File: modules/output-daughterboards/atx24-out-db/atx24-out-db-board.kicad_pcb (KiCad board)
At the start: 4 copper layers, 238 x 77 mm, 15 parts, among them J1 ATX24 OUT FIELD, J10 TE 63849-1, J11 TE 63849-1, J12 TE 63849-1, J13 TE 63849-1, J14 TE 63849-1, J15 TE 63849-1, J16 TE 63849-1, J17 TE 63849-1, J18 TE 63849-1, J20 SIGNAL STUB (2x5)

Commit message: WIP snapshot: daughterboard-projects agent in flight (durability)
Co-Authored-By: Claude Fable 5 <noreply@anthropic.com>
Claude-Session: https://claude.ai/code/session_01LvfqcnEeuin2oyJQw548EX
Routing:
- net +5V: track 138.7 -> 148.9 mm
- net +12V: track 66.2 -> 71.3 mm
- net +5VSB: track 49.1 -> 54.2 mm
- net +3V3: track 114.7 -> 119.8 mm

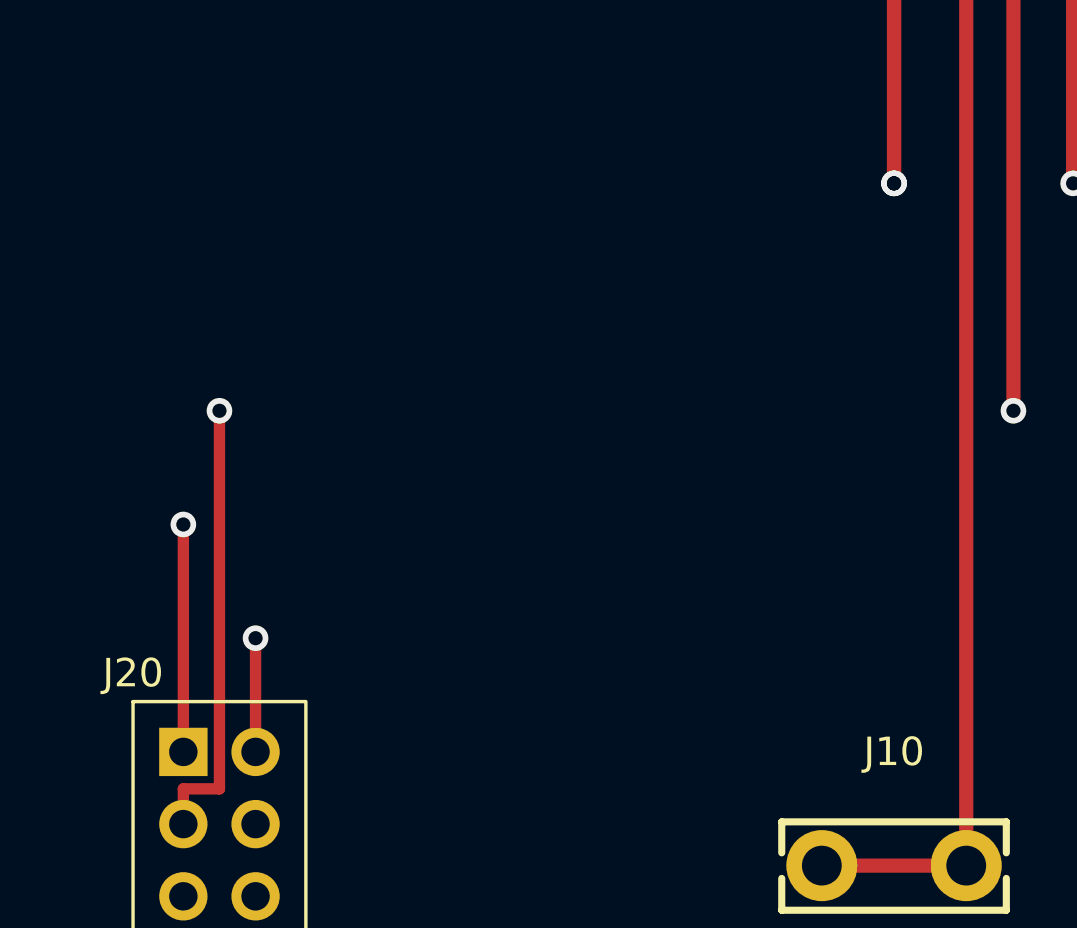
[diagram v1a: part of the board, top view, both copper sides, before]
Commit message: Task 10: output-daughterboard projects landed (atx24/eps/pcie, SS2.8 v1.4.0)
Three passive per-cable boards: TE 63849-1 tabs mapped 1:1 to the main
boards' TB order (a pin swap caught+fixed by cross-ref), full TH output
fields (24-circuit ATX / EPS 4+4 / PCIe 3+3+2sense-tied-GND), asymmetric
keying verified programmatically distinct across families, M3 chassis
mounts. 4-layer 2oz: EPS/PCIe = zero-track pure-pour 2-net boards; atx24 =
8-net In2 band routing (stale-netlist silent-reassignment bug found+fixed).
ERC 0 errors / DRC 0 at every severity, netlist-verified by
check_output_daughterboards.py. MODDIY not invented (OQ-88 provenance);
sense-return provisioned only (box e open). New lib assets + parametric
generator + check script.

Co-Authored-By: Claude Fable 5 <noreply@anthropic.com>
Claude-Session: https://claude.ai/code/session_01LvfqcnEeuin2oyJQw548EX
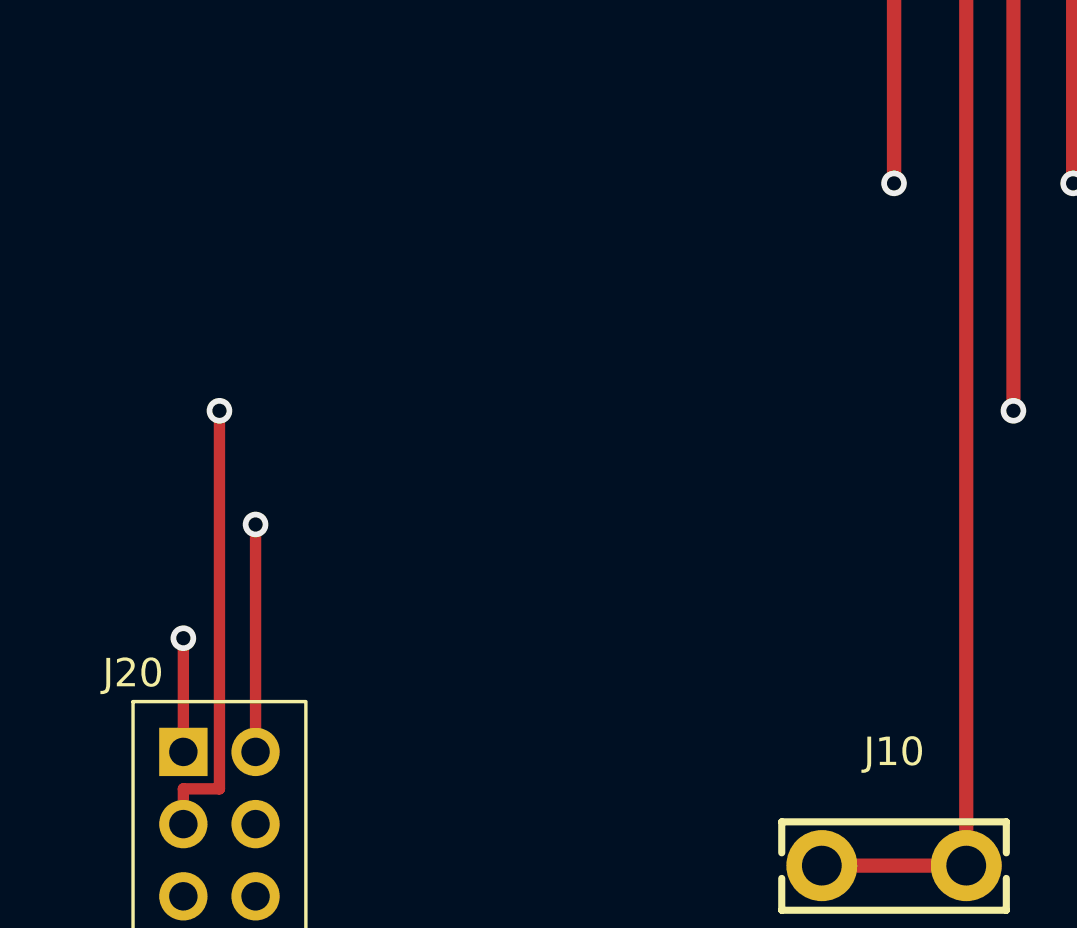
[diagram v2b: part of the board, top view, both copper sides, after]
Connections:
- J20 pad 1: /PWR_OK -> /PS_ON#
- J20 pad 2: /PS_ON# -> /PWR_OK
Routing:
- net +3V3: vias 5 -> 4

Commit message: Bench-mode Max addendum: T1 carries continuous telemetry, bursts for raw; GOWIN+P4 hub shape
Sustained budget 180-900 kB/s (10-50kHz/ch decimated) = 1.6-8% of one
100BASE-T1 link; fast-path raw-window bursts land <1s; continuous instrument
raw (100-260 MB/s at the ruled ADC options) exceeds every link class incl.
1000BASE-T1 — the ruled shape stays burst-into-memory, matching SS6.11's own
framing. Max hub ranked: GOWIN GW5A + P4 (owner prototype lineage) >
PolarFire ENT-posture variant > P4-only (OQ-20 caps N=1). GbE/RGMII egress
over USB HS at N=8. Freshness gaps corroborated (SS6.11 retired mux array +
debunked 2-5MHz band already owner-pen-tracked; phantom 'companion FPGA-Max
doc' cited 3x, absent). 8 owner questions incl. a REAL mismatch: owner fast
ADC = two CURRENT pairs (shunt+coil) vs the June-11 ruling's voltage+current
— where does the ATX-ripple VOLTAGE channel live?

Co-Authored-By: Claude Fable 5 <noreply@anthropic.com>
Claude-Session: https://claude.ai/code/session_01LvfqcnEeuin2oyJQw548EX
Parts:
- removed H1, H2, H3, H4: MountingHole_3.2mm_M3_Pad_Via, cec-MountingHole:MountingHole_3.2mm_M3_Pad_Via
- moved J18 145.1 mm to (73.8, 15.0)
- moved J17 144.7 mm to (65.2, 15.0)
- moved J16 144.3 mm to (56.6, 15.0)
- moved J15 143.9 mm to (48.0, 15.0)
- moved J14 129.5 mm to (39.4, 15.0)
- moved J13 115.2 mm to (30.8, 15.0)
- moved J12 101.4 mm to (22.2, 15.0)
- moved J11 101.0 mm to (13.6, 15.0)
- moved J20 62.9 mm to (56.6, 6.77), turned to 90 degrees
- moved J10 61.7 mm to (4.96, 15.0)
- moved J1 42.7 mm to (4.10, 2.75)
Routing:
- net +5V: track 148.9 -> 47.1 mm
- net +3V3: track 119.8 -> 42.8 mm
- net +12V: track 71.3 -> 29.9 mm
- net +5VSB: track 54.2 -> 19.5 mm
- net /-12V: track 41.3 -> 9.88 mm
- net /PS_ON#: track 37.5 -> 11.5 mm
- net /PWR_OK: track 45.1 -> 21.3 mm
- added copper zone on B.Cu, net +5V
- added copper zone on B.Cu, net +5VSB
- added copper zone on B.Cu, net /PWR_OK
- removed copper zone on In2.Cu, net +5V
- removed copper zone on In2.Cu, net +5VSB
- removed copper zone on In2.Cu, net /PWR_OK
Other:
- board size 238 x 77 mm -> 78.7 x 17 mm

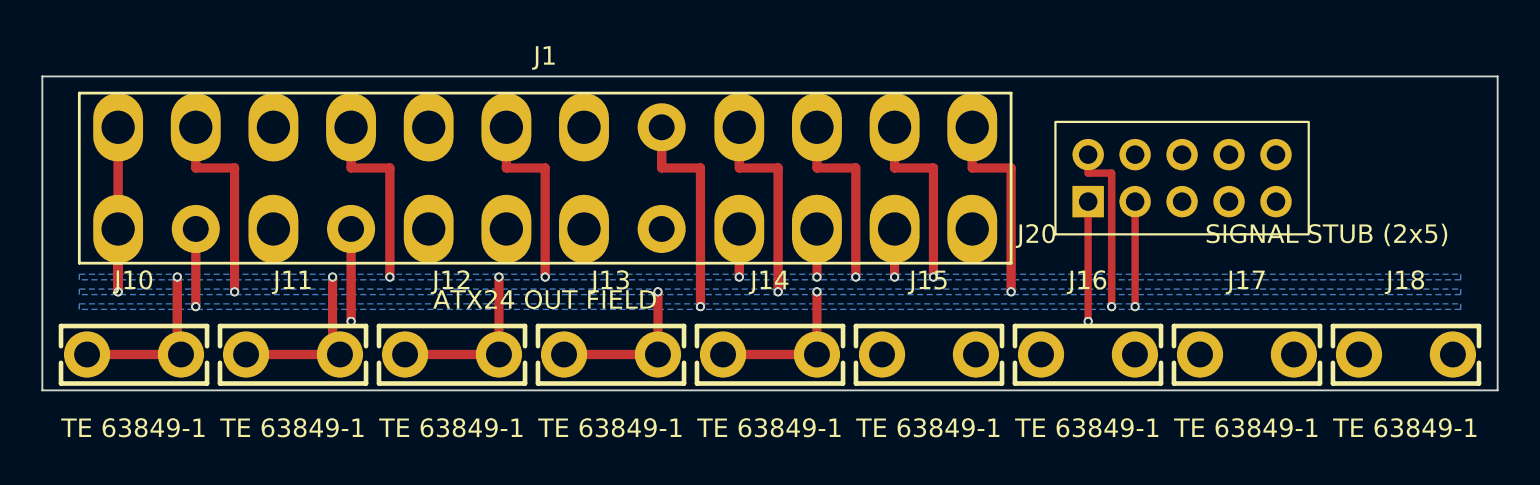
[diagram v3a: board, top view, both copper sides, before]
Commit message: WIP snapshot: shrink + voltage-path agents in flight (durability)
Co-Authored-By: Claude Fable 5 <noreply@anthropic.com>
Claude-Session: https://claude.ai/code/session_01LvfqcnEeuin2oyJQw548EX
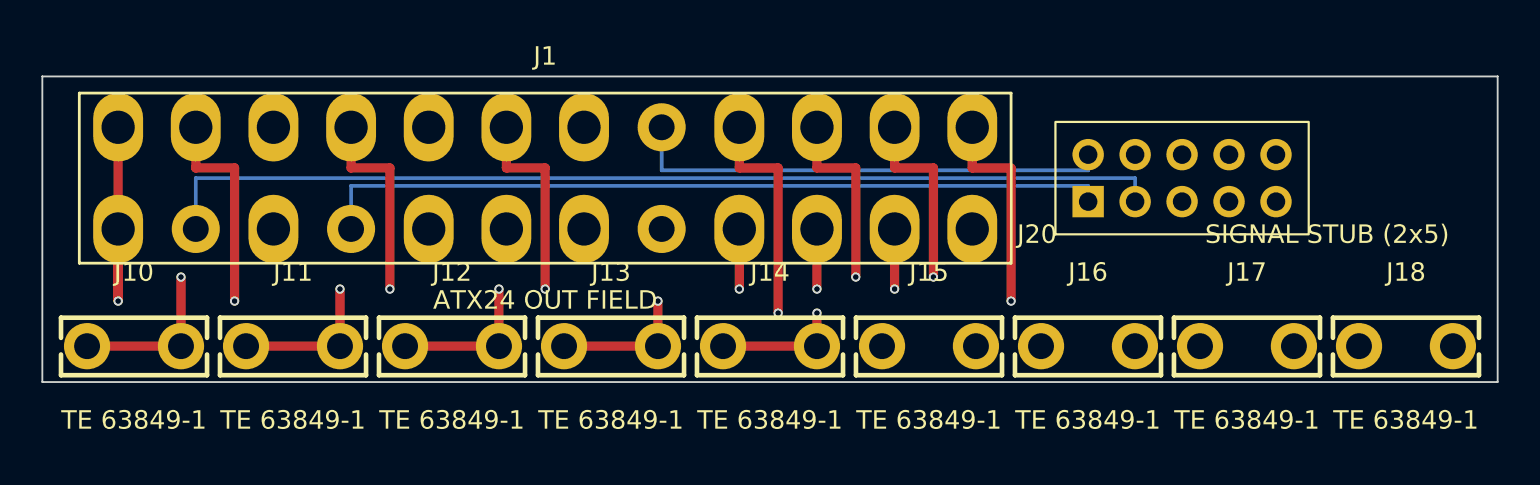
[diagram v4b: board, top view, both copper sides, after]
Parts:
- moved J10 0.45 mm to (4.96, 14.6)
- moved J11 0.45 mm to (13.6, 14.6)
- moved J12 0.45 mm to (22.2, 14.6)
- moved J13 0.45 mm to (30.8, 14.6)
- moved J14 0.45 mm to (39.4, 14.6)
- moved J15 0.45 mm to (48.0, 14.6)
- moved J16 0.45 mm to (56.6, 14.6)
- moved J17 0.45 mm to (65.2, 14.6)
- moved J18 0.45 mm to (73.8, 14.6)
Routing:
- net /-12V: track 9.88 -> 54.8 mm, vias 2 -> 0
- net /PS_ON#: track 11.5 -> 43.1 mm, vias 2 -> 0
- net /PWR_OK: track 21.3 -> 26.2 mm, vias 2 -> 0
- net +3V3: track 42.8 -> 43.8 mm
- net +5V: track 47.1 -> 47.8 mm
- net +12V: track 29.9 -> 29.2 mm
- added copper zone on In2.Cu, net +5V
- added copper zone on In2.Cu, net +5VSB
- removed copper zone on B.Cu, net +5V
- removed copper zone on B.Cu, net +5VSB
- removed copper zone on In2.Cu, net /-12V
- removed copper zone on In2.Cu, net /PS_ON#
- removed copper zone on B.Cu, net /PWR_OK
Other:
- board size 78.7 x 17 mm -> 78.7 x 16.5 mm

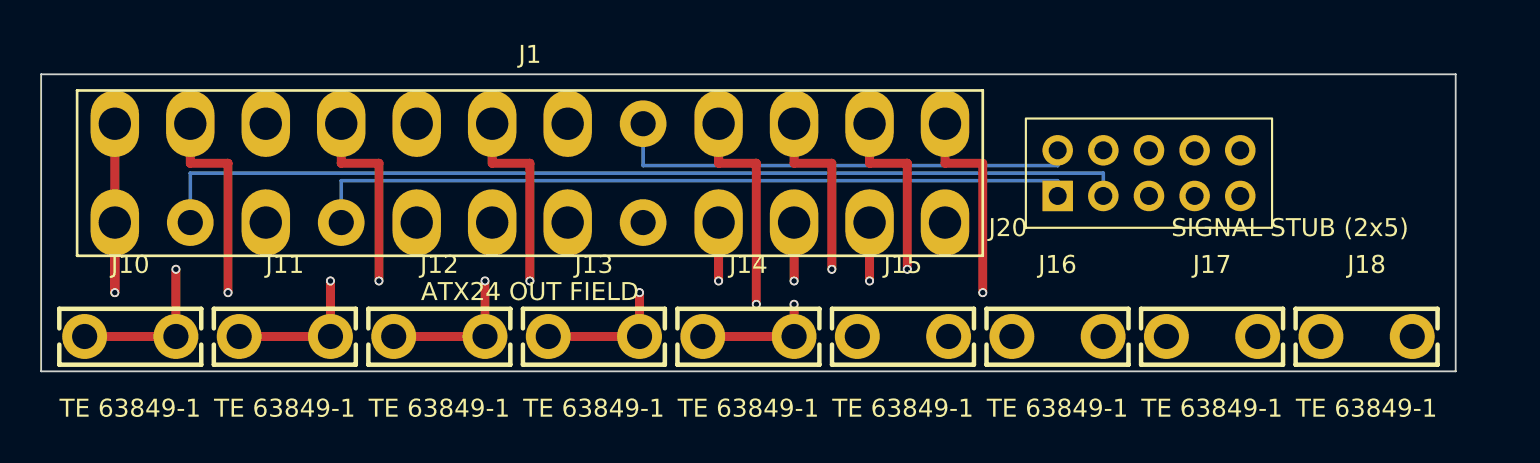
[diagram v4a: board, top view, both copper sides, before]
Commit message: Bench-mode SS7: voltage-path analysis + slow-path ceiling math (owner datasheet)
INA240 verified 400kHz -3dB flat across gains w/ 100kHz 2%-THD clean ceiling;
CSS2H R-series publishes only '<2nH' (no typ/curve) -> corner bracket
53-318kHz, consistent w/ the platform's 79.6kHz figure — BOTH caps land
~80-100kHz, neither dominates; production slow path ~1.6-2x prototype raw /
8-10x usable, gated on the OQ-21 ADC. RECOMMENDATION: fast-path VOLTAGE
(ATX ripple = the fast channel's own headline use case); across-connector
differential-V microarc observable = checked against the arc/phenomenology
corpus and NOVEL. Owner arc-recap + prototype-artifact framing recorded
verbatim; open questions extended (9-11).

Co-Authored-By: Claude Fable 5 <noreply@anthropic.com>
Claude-Session: https://claude.ai/code/session_01LvfqcnEeuin2oyJQw548EX
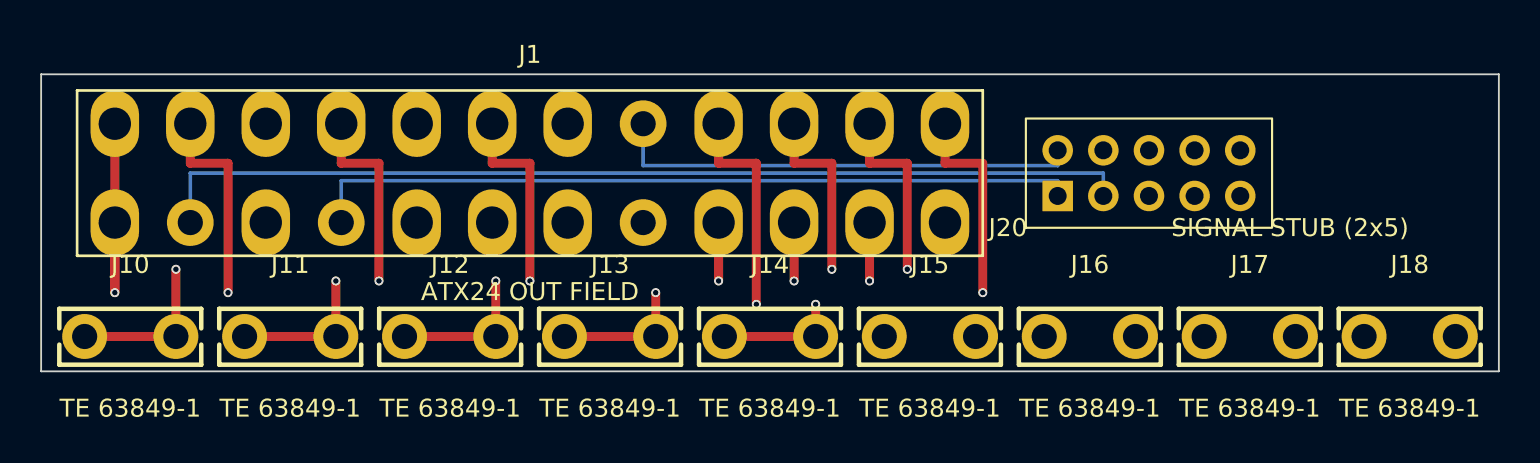
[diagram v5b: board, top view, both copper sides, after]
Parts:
- moved J18 2.40 mm to (76.2, 14.6)
- moved J17 2.10 mm to (67.3, 14.6)
- moved J16 1.80 mm to (58.4, 14.6)
- moved J15 1.50 mm to (49.5, 14.6)
- moved J14 1.20 mm to (40.6, 14.6)
- moved J13 0.90 mm to (31.7, 14.6)
- moved J12 0.60 mm to (22.8, 14.6)
- moved J11 0.30 mm to (13.9, 14.6)
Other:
- board size 78.7 x 16.5 mm -> 81.1 x 16.5 mm

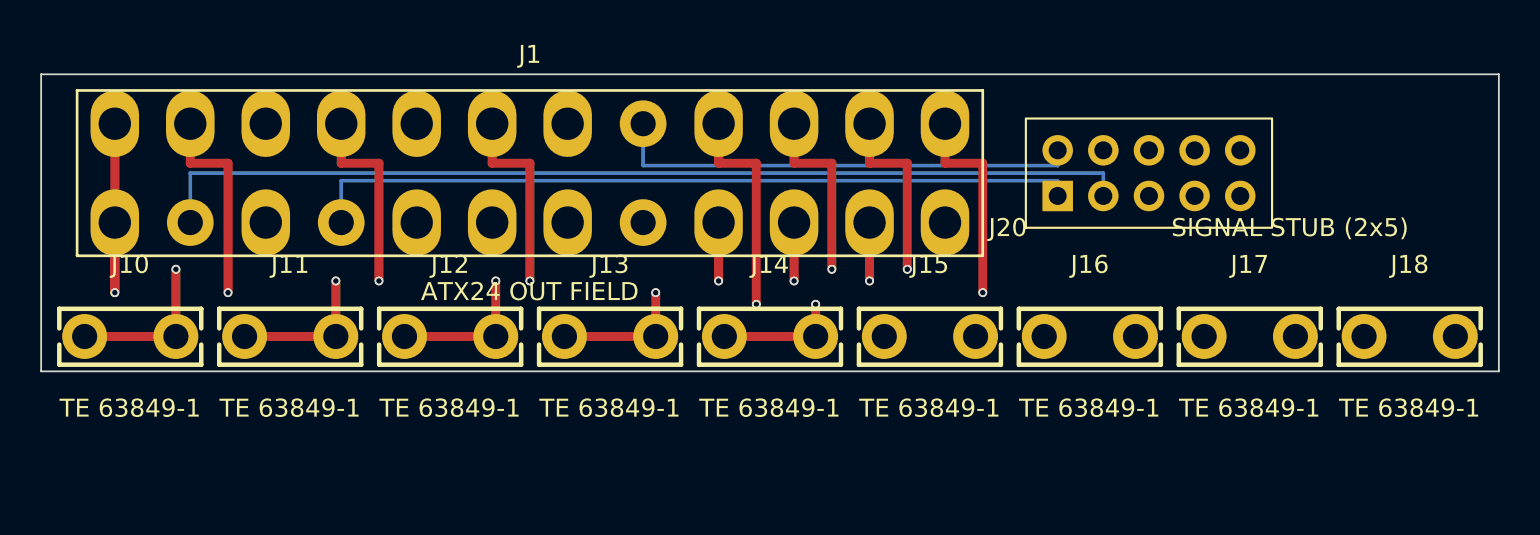
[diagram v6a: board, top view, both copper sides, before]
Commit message: WIP snapshot: flat-tab agent regenerating daughterboards onto TE 63951-1 (durability; verification pending)
Co-Authored-By: Claude Fable 5 <noreply@anthropic.com>
Claude-Session: https://claude.ai/code/session_01LvfqcnEeuin2oyJQw548EX
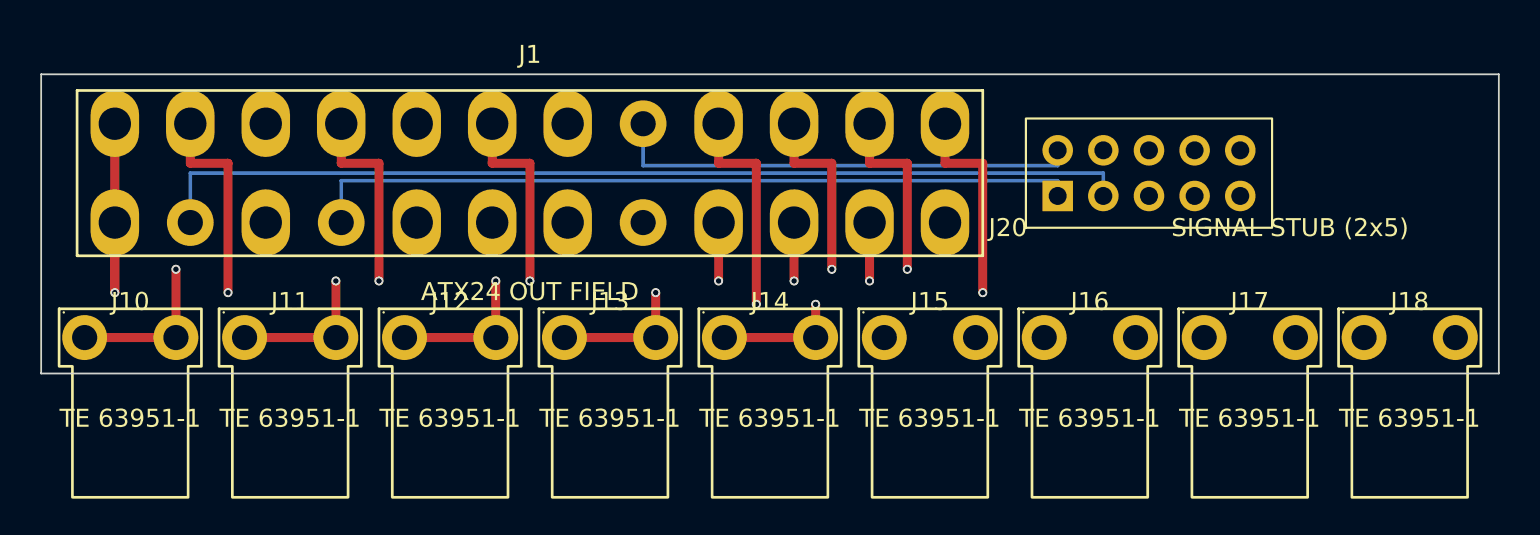
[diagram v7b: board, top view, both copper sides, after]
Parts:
- J10, J11, J12, J13, J14, J15, J16, J17, J18: value TE 63849-1 -> TE 63951-1; footprint cec-Connector_Blade:TE_63849-1_FASTON_Tab_250x032_THT -> cec-Connector_Blade:TE_63951-1_FASTON_Tab_250x032_RA_THT
- moved J10 0.06 mm to (4.96, 14.7)
- moved J11 0.06 mm to (13.9, 14.7)
- moved J12 0.06 mm to (22.8, 14.7)
- moved J13 0.06 mm to (31.7, 14.7)
- moved J14 0.06 mm to (40.6, 14.7)
- moved J15 0.06 mm to (49.5, 14.7)
- moved J16 0.06 mm to (58.4, 14.7)
- moved J17 0.06 mm to (67.3, 14.7)
- moved J18 0.06 mm to (76.2, 14.7)
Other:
- board size 81.1 x 16.5 mm -> 81.1 x 16.6 mm
